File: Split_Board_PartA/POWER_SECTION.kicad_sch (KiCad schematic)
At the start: 25 parts, among them J6 Conn_01x10, U36 LM1117-3.3

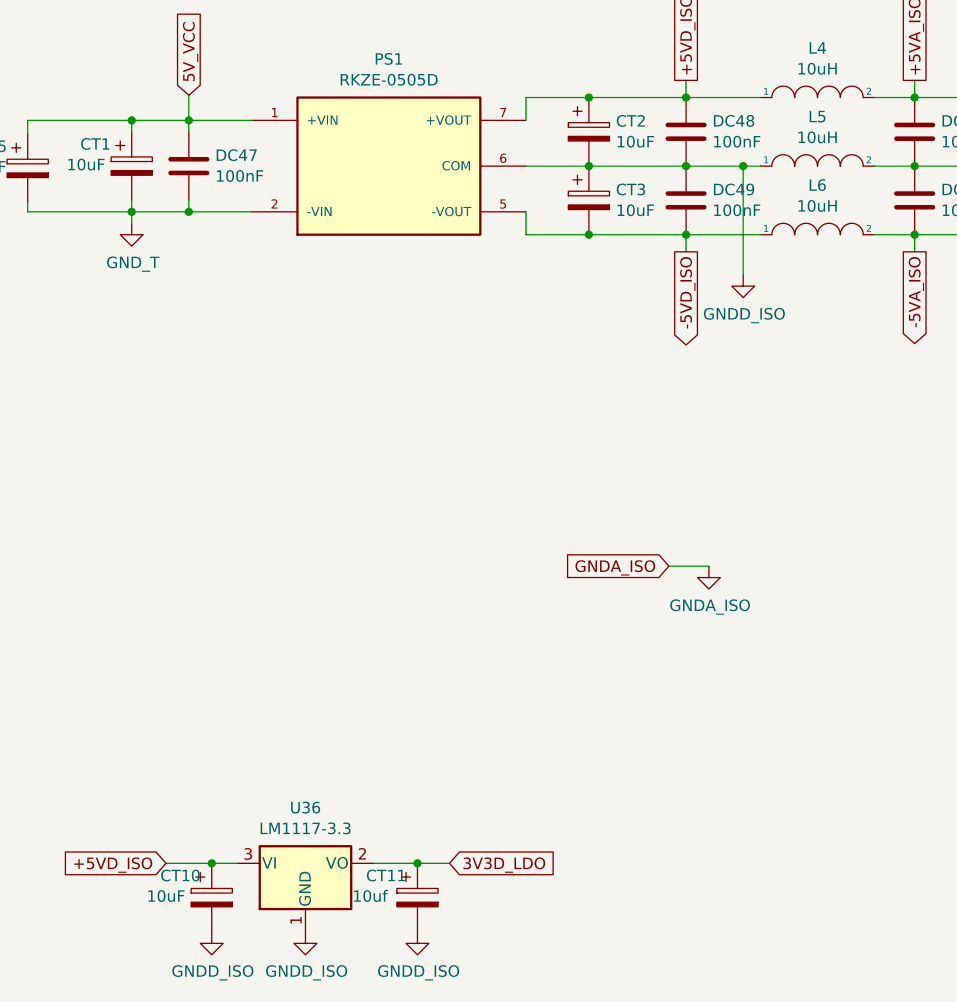
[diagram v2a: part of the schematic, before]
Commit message: eliminated the GNDD_ISO net
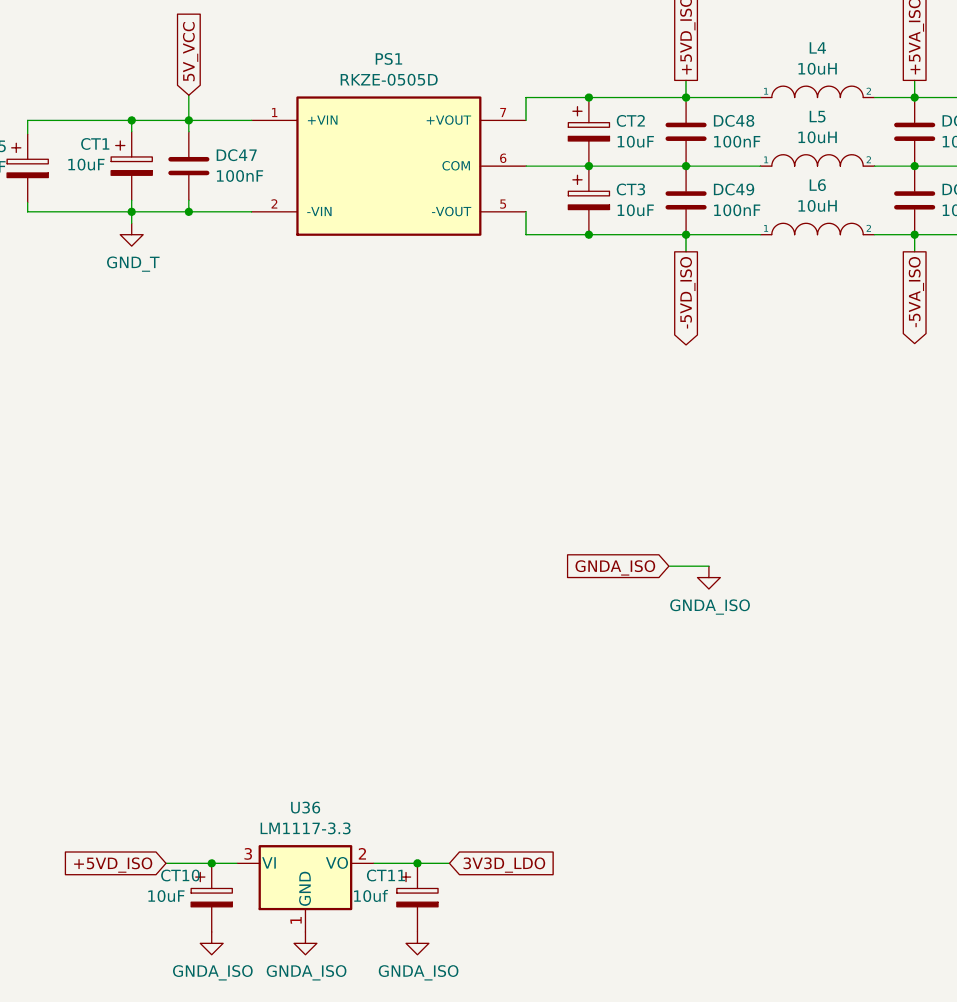
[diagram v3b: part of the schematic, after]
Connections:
- net GNDD_ISO: no longer CT2.2, CT3.1, DC48.2, DC49.1, L5.1, PS1.6 (COM)
- new net: CT2.2, CT3.1, DC48.2, DC49.1, L5.1, PS1.6 (COM)
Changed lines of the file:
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@@
   (junction (at 138.43 53.975) (diameter 0) (color 0 0 0 0)
   )
-  (junction (at 119.38 53.975) (diameter 0) (color 0 0 0 0)
-  )
   (wire (pts (xy 55.245 131.445) (xy 60.325 131.445))
     (stroke (width 0) (type default))
@@
     (stroke (width 0) (type default))
   )
-  (wire (pts (xy 113.03 53.975) (xy 119.38 53.975))
-    (stroke (width 0) (type default))
-  )
   (wire (pts (xy 113.03 61.595) (xy 121.285 61.595))
     (stroke (width 0) (type default))
@@
     (stroke (width 0) (type default))
   )
-  (wire (pts (xy 119.38 53.975) (xy 119.38 66.04))
-    (stroke (width 0) (type default))
-  )
   (wire (pts (xy 63.119 131.445) (xy 60.325 131.445))
     (stroke (width 0) (type default))
@@
     (stroke (width 0) (type default))
   )
-  (wire (pts (xy 119.38 53.975) (xy 121.285 53.975))
+  (wire (pts (xy 113.03 53.975) (xy 121.285 53.975))
     (stroke (width 0) (type default))
   )
@@
       (effects (font (size 1.27 1.27)) hide)
     )
-    (property "Value" "GNDD_ISO" (at 83.312 143.4592 0)
+    (property "Value" "GNDA_ISO" (at 83.312 143.4592 0)
       (effects (font (size 1.27 1.27)))
     )
@@
     )
   )
-  (symbol (lib_id "ohm3000Board-rescue:GNDD_ISO-power") (at 119.38 66.04 0) (unit 1)
-    (in_bom yes) (on_board yes) (dnp no)
-    (property "Reference" "#PWR0105" (at 119.38 72.39 0)
-      (effects (font (size 1.27 1.27)) hide)
-    )
-    (property "Value" "GNDD_ISO" (at 119.507 70.4342 0)
-      (effects (font (size 1.27 1.27)))
-    )
-    (property "Footprint" "" (at 119.38 66.04 0)
-      (effects (font (size 1.27 1.27)) hide)
-    )
-    (property "Datasheet" "" (at 119.38 66.04 0)
-      (effects (font (size 1.27 1.27)) hide)
-    )
-    (pin "1")
-    (instances
-      (project "ohm3000_ISO_Board"
-        (path "/cc48dd41-7768-48d3-b096-2c4cc2126c9d/00000000-0000-0000-0000-000060321a4f"
-          (reference "#PWR0105") (unit 1)
-        )
-      )
-      (project "Split_Board_PartA"
-        (path "/d606f975-4fc9-446c-a768-86bfd0ba9f6c/96c878e7-e6c5-471d-934c-d33573418638"
-          (reference "#PWR046") (unit 1)
-        )
-      )
-    )
-  )
   (symbol (lib_id "Mechanical:MountingHole") (at 219.583 141.986 0) (unit 1)
     (in_bom yes) (on_board yes) (dnp no)
@@
       (effects (font (size 1.27 1.27)) hide)
     )
-    (property "Value" "GNDD_ISO" (at 60.452 143.4592 0)
+    (property "Value" "GNDA_ISO" (at 60.452 143.4592 0)
       (effects (font (size 1.27 1.27)))
     )
@@
       (effects (font (size 1.27 1.27)) hide)
     )
-    (property "Value" "GNDD_ISO" (at 70.866 143.4592 0)
-      (effects (font (size 1.27 1.27)))
-    )
+    (property "Value" "GNDA_ISO" (at 70.866 143.4592 0)
+      (effects (font (size 1.27 1.27)))
+    )
